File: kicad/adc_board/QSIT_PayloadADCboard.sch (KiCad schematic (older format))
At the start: 34 parts, among them J1 Conn_02x05_Odd_Even, J2 Conn_02x05_Odd_Even, J3 Conn_02x05_Odd_Even, U1 MCP3561_4CH, U2 NCP1117-3.3_SOT223

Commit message: changed to single 9pin connector
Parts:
- removed J1, J2, J3: Conn_02x05_Odd_Even, Connector_PinSocket_1.27mm:PinSocket_2x05_P1.27mm_Vertical_SMD, symbol Connector_Generic:Conn_02x05_Odd_Even
- removed JP1, JP2, JP3: bridge, Jumper:SolderJumper-3_P1.3mm_Open_RoundedPad1.0x1.5mm, symbol Jumper:Jumper_3_Bridged12
- removed U1: MCP3561_4CH, Package_SO:TSSOP-20_4.4x6.5mm_P0.65mm, symbol A_Tale_Of_A_Library:MCP3561_4CH
- removed U2: NCP1117-3.3_SOT223, Package_TO_SOT_SMD:SOT-223-3_TabPin2, symbol Regulator_Linear:NCP1117-3.3_SOT223
- removed VR1: LM4040D25FTA, digikey-footprints:SOT-23-3, symbol dk_PMIC-Voltage-Reference:LM4040D25FTA
- added C10, C11, C12, C13, C14, C15, C9: 100nF, Capacitor_SMD:C_0603_1608Metric_Pad1.05x0.95mm_HandSolder, symbol Device:C
- added C16, C18: 4u7, Capacitor_THT:CP_Radial_D4.0mm_P2.00mm, symbol Device:CP
- added C17: 2u2, Capacitor_THT:CP_Radial_D4.0mm_P2.00mm, symbol Device:CP
- added C? (x2): 12p, Capacitor_SMD:C_0603_1608Metric_Pad1.05x0.95mm_HandSolder, symbol Device:C
- added D1, D2: LED, LED_SMD:LED_0805_2012Metric_Pad1.15x1.40mm_HandSolder, symbol Device:LED
- added J1: Conn_01x09, Connector_PinHeader_2.54mm:PinHeader_1x09_P2.54mm_Vertical, symbol Connector_Generic:Conn_01x09
- added J2: Power_Conn, TerminalBlock_4Ucon:TerminalBlock_4Ucon_1x02_P3.50mm_Horizontal, symbol Connector:Screw_Terminal_01x02
- added J4: Conn_ARM_JTAG_SWD_10, Connector_PinHeader_1.27mm:PinHeader_2x05_P1.27mm_Vertical_SMD, symbol Connector:Conn_ARM_JTAG_SWD_10
- added J5: Conn_01x03, Connector_PinHeader_2.54mm:PinHeader_1x03_P2.54mm_Vertical, symbol Connector_Generic:Conn_01x03
- added J6: Conn_02x05_Odd_Even, Connector_PinSocket_1.27mm:PinSocket_2x05_P1.27mm_Vertical_SMD, symbol Connector_Generic:Conn_02x05_Odd_Even
- added R12, R13, R16, R19, R? (x2): 10k, Resistor_SMD:R_0603_1608Metric_Pad1.05x0.95mm_HandSolder, symbol Device:R
- added R14, R15: 10R, Resistor_SMD:R_0603_1608Metric_Pad1.05x0.95mm_HandSolder, symbol Device:R
- added R17, R18: 330R, Resistor_SMD:R_0603_1608Metric_Pad1.05x0.95mm_HandSolder, symbol Device:R
- added SW1: SW_Push, Button_Switch_SMD:SW_Push_1P1T_NO_CK_KMR2, symbol Switch:SW_Push
- added U1: MCP3564, Package_SO:TSSOP-20_4.4x6.5mm_P0.65mm, symbol A_Tale_Of_A_Library:MCP3564
- added U2: MAX6070, Package_TO_SOT_SMD:SOT-23-6_Handsoldering, symbol A_Tale_Of_A_Library:MAX6070
- added U3: STM32F373CCT6, Package_QFP:LQFP-48_7x7mm_P0.5mm, symbol MCU_ST_STM32F3:STM32F373CCTx
- added U4: TC1108-3.3VDBTR, Package_TO_SOT_SMD:SOT-223-3_TabPin2, symbol Regulator_Linear:LT1129-3.3_SOT223
- added U5: MPE1205S-1W, A_Tale_Of_A_Library:Converter_DCDC_multicorp_THT, symbol A_Tale_Of_A_Library:MPE1205S-1W
- added X?: ECS-2520MVLC-049-BN, Oscillator:Oscillator_SMD_ECS_2520MV-xxx-xx-4Pin_2.5x2.0mm, symbol Oscillator:ECS-2520MV-xxx-xx
- added Y?: 8MHz, symbol Device:Crystal
- C1, C2, C3, C4, C5, C6, C7, C8: Type (none) -> X7R; Voltage (none) -> 16V
- R1: value R -> 10R
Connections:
- net labels added: +12V, ADC_CH1, ADC_CH2, ADC_CH3, ADC_CH4, BOOT0, BOOT1, FCLK_X, FCLK_Y, LED1, LED2, MEMS_OUT_EN, SPI1_CS, SPI1_MISO, SPI1_MOSI, SPI1_SCK, SPI1_~IRQ~, SPI2_CS, SPI2_MOSI, SPI2_SCK, SWCLK, SWDIO, TIM14_CH1, TIM16_CH1, TIM17_CH1, USART2_RX, USART2_TX, VAA, ~RST
- net labels removed: MISO, MOSI, SCK, U_signal, X1a, X2a, X_signal, Y1a, Y2a, Y_signal, ~CS, ~IRQ
- wire segments 95 -> 187
- no-connect marks 2 -> 5
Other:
- note added: "2.5V Reference"
- note added: "2.5V ±2ppm/°C"
- note added: "240 Hz x 60 = 14.4 kHz"
- note added: "300mA out"
- note added: "9P flat cable"
- note added: "ARM SWD Connector"
- note added: "Analog"
- note added: "Debug"
- note added: "Input Voltage\n10.8 ... 13.2"
- note added: "MCLK 4.9152 MHz generator"
- note added: "MCU"
- note added: "MEMS Driver"
- note added: "MPE1205S-1W\nIsol. DC/DC, THT, 1 W, +/-5 V, 100mA\n"
- note added: "Mechanical"
- note added: "Power"
- note added: "UART (Debug)"
- note added: "add power switch for MEMS driver?"
- note added: "pinout see:\nMirrorcle BDQ PicoAmp 4.6 User Guide.pdf"
- note removed: "- check ISE for 2.5 reference\n- check ISE for +/- 5V DC source\n- check ISE for 3.3V regulator\n- find out, if more stuff fits on a larger PCB\n- research Pinout of Mirrorcle Board"
- note removed: "60uA ... 15mA bias current"
- note removed: "The LM4040 does not require an external stabilizing \ncapacitor while ensuring stability with any capacitive load."
- note removed: "do not use STM32 (not in stock)\ndo not use internal ADCs because min. 14 Bit resolution is required\nuse flat cable to connect to a Teensy breakout board"
- moved on the sheet: C1, C2, C3, C4, C5, C6, C7, C8, FB1, H1, H2, H3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

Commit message: STM32 board ready for review
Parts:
- removed R3: 10R, Resistor_SMD:R_0603_1608Metric_Pad1.05x0.95mm_HandSolder, symbol Device:R
- removed R?: 10k, Resistor_SMD:R_0603_1608Metric_Pad1.05x0.95mm_HandSolder, symbol Device:R
- removed Y?: 8MHz, symbol Device:Crystal
- added TP1: TestPoint, TestPoint:TestPoint_Keystone_5000-5004_Miniature, symbol Connector:TestPoint
- added Y1: Crystal_GND24, Crystal:Crystal_SMD_TXC_7M-4Pin_3.2x2.5mm, symbol Device:Crystal_GND24
- gave numbers to parts that had none: 4
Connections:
- net BOOT0: now also TP1.1
- net GND: now also Y1.2, Y1.4
- net MCLK: now also U1.18 (MCLKIN)
- net MEMS_OUT_EN: now also U3.29 (PA8)
- net at C19.1, U3.5 (PF0): now also Y1.1
- net at C20.1, U3.6 (PF1): now also Y1.3
- net BOOT1: no longer names the net of U3.20 (PB2)
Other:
- note added: "BOOT1 BOOT0 \n x 0 flash memory\n 0 1 system memory\n 1 1 embedded SRAM"
- note added: "double check pinout"
- note added: "https://www.digikey.ch/de/products/detail/olimex-ltd/ARM-JTAG-20-10/3471401"
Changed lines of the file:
@@
 	0    -1   -1   0
 $EndComp
-$Comp
-L Device:R R3
-U 1 1 61A6A943
-P 7700 1150
-F 0 "R3" V 7750 1350 50  0000 C CNN
-F 1 "10R" V 7700 1150 50  0000 C CNN
-F 2 "Resistor_SMD:R_0603_1608Metric_Pad1.05x0.95mm_HandSolder" V 7630 1150 50  0001 C CNN
-F 3 "~" H 7700 1150 50  0001 C CNN
-	1    7700 1150
-	0    -1   -1   0
-$EndComp
 Wire Wire Line
 	1100 6250 1100 6200
@@
 Wire Wire Line
 	5050 5500 4850 5500
-Text GLabel 7150 5000 2    50   Input ~ 0
-BOOT1
 Wire Wire Line
 	6450 4900 6650 4900
@@
 9P flat cable
 $Comp
-L Device:R R?
+L Device:R R20
 U 1 1 623954BA
 P 4750 3550
-F 0 "R?" H 4900 3600 50  0000 L CNN
+F 0 "R20" H 4900 3600 50  0000 L CNN
 F 1 "10k" H 4820 3505 50  0000 L CNN
 F 2 "Resistor_SMD:R_0603_1608Metric_Pad1.05x0.95mm_HandSolder" V 4680 3550 50  0001 C CNN
@@
 Wire Wire Line
 	5050 3400 4750 3400
-Wire Wire Line
-	4750 3400 4550 3400
 Connection ~ 4750 3400
 $Comp
-L power:GND #PWR?
+L power:GND #PWR041
 U 1 1 623ABA27
 P 4750 3700
-F 0 "#PWR?" H 4750 3450 50  0001 C CNN
+F 0 "#PWR041" H 4750 3450 50  0001 C CNN
 F 1 "GND" H 4850 3550 50  0000 R CNN
 F 2 "" H 4750 3700 50  0001 C CNN
@@
 	1    0    0    -1
 $EndComp
-Text GLabel 4550 3400 0    50   Input ~ 0
+Text GLabel 4300 3400 0    50   Input ~ 0
 BOOT0
-$Comp
-L Device:R R?
-U 1 1 623C7134
-P 6900 5100
-F 0 "R?" V 6850 5250 50  0000 L CNN
-F 1 "10k" V 6900 5050 50  0000 L CNN
-F 2 "Resistor_SMD:R_0603_1608Metric_Pad1.05x0.95mm_HandSolder" V 6830 5100 50  0001 C CNN
-F 3 "~" H 6900 5100 50  0001 C CNN
-	1    6900 5100
-	0    1    -1   0
-$EndComp
-Wire Wire Line
-	6750 5100 6700 5100
-Wire Wire Line
-	6700 5100 6650 5050
-Wire Wire Line
-	7050 5100 7250 5100
-$Comp
-L power:GND #PWR?
-U 1 1 623E97D1
-P 7250 5100
-F 0 "#PWR?" H 7250 4850 50  0001 C CNN
-F 1 "GND" V 7250 4950 50  0000 R CNN
-F 2 "" H 7250 5100 50  0001 C CNN
-F 3 "" H 7250 5100 50  0001 C CNN
-	1    7250 5100
-	0    -1   -1   0
-$EndComp
 Text Notes 1250 3500 0    50   ~ 0
 MCLK 4.9152 MHz generator
 $Comp
-L Oscillator:ECS-2520MV-xxx-xx X?
+L Oscillator:ECS-2520MV-xxx-xx X1
 U 1 1 61AAE6AA
 P 1150 3750
-F 0 "X?" H 1550 3600 50  0000 L CNN
+F 0 "X1" H 1550 3600 50  0000 L CNN
 F 1 "ECS-2520MVLC-049-BN" H 1300 3450 50  0000 L CNN
 F 2 "Oscillator:Oscillator_SMD_ECS_2520MV-xxx-xx-4Pin_2.5x2.0mm" H 1600 3400 50  0001 C CNN
@@
 $EndComp
 $Comp
-L power:+3V3 #PWR?
+L power:+3V3 #PWR040
 U 1 1 61AB5159
 P 1150 3450
-F 0 "#PWR?" H 1150 3300 50  0001 C CNN
+F 0 "#PWR040" H 1150 3300 50  0001 C CNN
 F 1 "+3V3" H 1150 3600 50  0000 C CNN
 F 2 "" H 1150 3450 50  0001 C CNN
@@
 $EndComp
 $Comp
-L power:GND #PWR?
+L power:GND #PWR042
 U 1 1 61AB6346
 P 1150 4050
-F 0 "#PWR?" H 1150 3800 50  0001 C CNN
+F 0 "#PWR042" H 1150 3800 50  0001 C CNN
 F 1 "GND" H 1250 3900 50  0000 R CNN
 F 2 "" H 1150 4050 50  0001 C CNN
@@
 NoConn ~ 750  3750
 Wire Wire Line
-	7450 1150 7550 1150
-Wire Wire Line
 	7450 1250 7950 1250
 Wire Wire Line
@@
 	7950 1450 7450 1450
 Wire Wire Line
-	7850 1150 8250 1150
-Wire Wire Line
 	8250 1350 7850 1350
 Wire Wire Line
@@
 	2950 5200 2700 5200
 $Comp
-L Device:Crystal Y?
-U 1 1 61DA8492
-P 4400 4450
-F 0 "Y?" V 4354 4581 50  0000 L CNN
-F 1 "8MHz" V 4445 4581 50  0000 L CNN
-F 2 "" H 4400 4450 50  0001 C CNN
-F 3 "~" H 4400 4450 50  0001 C CNN
-	1    4400 4450
-	0    1    1    0
-$EndComp
-$Comp
-L Device:C C?
+L Device:C C19
 U 1 1 61DC61B7
 P 4200 4300
-F 0 "C?" V 4000 4450 50  0000 C CNN
+F 0 "C19" V 4000 4450 50  0000 C CNN
 F 1 "12p" V 4100 4450 50  0000 C CNN
 F 2 "Capacitor_SMD:C_0603_1608Metric_Pad1.05x0.95mm_HandSolder" H 4238 4150 50  0001 C CNN
@@
 $EndComp
 $Comp
-L Device:C C?
+L Device:C C20
 U 1 1 61DC7D49
 P 4200 4600
-F 0 "C?" V 4000 4750 50  0000 C CNN
+F 0 "C20" V 4000 4750 50  0000 C CNN
 F 1 "12p" V 4100 4750 50  0000 C CNN
 F 2 "Capacitor_SMD:C_0603_1608Metric_Pad1.05x0.95mm_HandSolder" H 4238 4450 50  0001 C CNN
@@
 $EndComp
 Wire Wire Line
-	4400 4600 4350 4600
-Wire Wire Line
-	4400 4300 4350 4300
-Wire Wire Line
 	4050 4300 4050 4450
 $Comp
-L power:GND #PWR?
+L power:GND #PWR043
 U 1 1 61DE5BC5
 P 4050 4450
-F 0 "#PWR?" H 4050 4200 50  0001 C CNN
+F 0 "#PWR043" H 4050 4200 50  0001 C CNN
 F 1 "GND" V 4050 4300 50  0000 R CNN
 F 2 "" H 4050 4450 50  0001 C CNN
@@
 Wire Wire Line
 	4050 4450 4050 4600
-Connection ~ 4400 4600
 $Comp
 L MCU_ST_STM32F3:STM32F373CCTx U3
@@
 $EndComp
 Wire Wire Line
-	5050 4700 4900 4700
-Wire Wire Line
-	4900 4700 4850 4650
-Wire Wire Line
-	4850 4650 4850 4350
-Wire Wire Line
-	4850 4350 4800 4300
-Wire Wire Line
-	4800 4300 4400 4300
-Connection ~ 4400 4300
-Wire Wire Line
 	4700 4600 4750 4650
 Wire Wire Line
@@
 Wire Wire Line
 	4800 4800 5050 4800
-Wire Wire Line
-	4400 4600 4700 4600
 NoConn ~ 1600 1450
 NoConn ~ 1600 1550
@@
 Wire Notes Line
 	600  7700 3300 7700
-Wire Wire Line
-	6450 5000 6650 5000
-Wire Wire Line
-	6650 5050 6650 5000
-Connection ~ 6650 5000
-Wire Wire Line
-	6650 5000 7150 5000
 Wire Notes Line
 	11100 6450 11100 4900
@@
 Mechanical
 $Comp
-L Graphic:SYM_Flash_Small #SYM?
+L Graphic:SYM_Flash_Small #SYM1
 U 1 1 62104C7E
 P 8150 5350
-F 0 "#SYM?" V 8060 5350 50  0001 C CNN
+F 0 "#SYM1" V 8060 5350 50  0001 C CNN
 F 1 "SYM_Flash_Small" V 8240 5350 50  0001 C CNN
 F 2 "" H 8150 5325 50  0001 C CNN
@@
 	1    0    0    -1
 $EndComp
+Wire Notes Line style solid
+	3700 3000 3700 3300
+Text Notes 3450 3300 0    50   ~ 0
+BOOT1 BOOT0 \n   x     0     flash memory\n   0     1     system memory\n   1     1     embedded SRAM
+Wire Notes Line style solid
+	4000 3000 4000 3300
+Wire Notes Line style solid
+	3450 3050 4650 3050
+$Comp
+L Connector:TestPoint TP1
+U 1 1 61B364E0
+P 4300 3500
+F 0 "TP1" V 4200 3600 50  0000 C CNN
+F 1 "TestPoint" V 4404 3572 50  0001 C CNN
+F 2 "TestPoint:TestPoint_Keystone_5000-5004_Miniature" H 4500 3500 50  0001 C CNN
+F 3 "~" H 4500 3500 50  0001 C CNN
+	1    4300 3500
+	0    -1   -1   0
+$EndComp
+Wire Wire Line
+	4300 3400 4450 3400
+Wire Wire Line
+	4300 3500 4350 3500
+Wire Wire Line
+	4350 3500 4450 3400
+Connection ~ 4450 3400
+Wire Wire Line
+	4450 3400 4750 3400
+Text Notes 1300 2300 0    39   ~ 0
+https://www.digikey.ch/de/products/detail/olimex-ltd/ARM-JTAG-20-10/3471401
+Text Notes 1650 1800 0    50   ~ 0
+double check pinout
+$Comp
+L Device:Crystal_GND24 Y1
+U 1 1 61C03ABE
+P 4450 4450
+F 0 "Y1" V 4650 4550 50  0000 L CNN
+F 1 "Crystal_GND24" V 4200 4500 50  0000 L CNN
+F 2 "Crystal:Crystal_SMD_TXC_7M-4Pin_3.2x2.5mm" H 4450 4450 50  0001 C CNN
+F 3 "~" H 4450 4450 50  0001 C CNN
+	1    4450 4450
+	0    1    1    0
+$EndComp
+Wire Wire Line
+	4350 4300 4450 4300
+Wire Wire Line
+	4350 4600 4450 4600
+Connection ~ 4450 4300
+Connection ~ 4450 4600
+Wire Wire Line
+	4250 4450 4050 4450
+Wire Wire Line
+	4450 4600 4700 4600
+$Comp
+L power:GND #PWR044
+U 1 1 61C17303
+P 4650 4450
+F 0 "#PWR044" H 4650 4200 50  0001 C CNN
+F 1 "GND" V 4650 4350 50  0000 R CNN
+F 2 "" H 4650 4450 50  0001 C CNN
+F 3 "" H 4650 4450 50  0001 C CNN
+	1    4650 4450
+	0    -1   -1   0
+$EndComp
+Wire Wire Line
+	5050 4700 5000 4700
+Wire Wire Line
+	5000 4700 4950 4650
+Wire Wire Line
+	4950 4650 4950 4350
+Wire Wire Line
+	4950 4350 4900 4300
+Wire Wire Line
+	4450 4300 4900 4300
+Wire Wire Line
+	7450 1150 8250 1150
+Text GLabel 6650 3900 2    50   Input ~ 0
+MEMS_OUT_EN
+Wire Wire Line
+	6650 3900 6450 3900
 $EndSCHEMATC

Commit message: further pcb improvements
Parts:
- removed C16, C18: 4u7, Capacitor_THT:CP_Radial_D4.0mm_P2.00mm, symbol Device:CP
- removed U1: MCP3564, Package_SO:TSSOP-20_4.4x6.5mm_P0.65mm, symbol A_Tale_Of_A_Library:MCP3564
- removed U2: MAX6070, Package_TO_SOT_SMD:SOT-23-6_Handsoldering, symbol A_Tale_Of_A_Library:MAX6070
- removed U5: MPE1205S-1W, A_Tale_Of_A_Library:Converter_DCDC_multicorp_THT, symbol A_Tale_Of_A_Library:MPE1205S-1W
- added C16, C18, C21: 4u7, Capacitor_SMD:C_1206_3216Metric, symbol Device:C
- added C22: 100nF, Capacitor_SMD:C_0603_1608Metric, symbol Device:C
- added U1: MCP3564, Package_SO:TSSOP-20_4.4x6.5mm_P0.65mm, symbol simonmartin_kicad_lib:MCP3564
- added U2: MAX6070, Package_TO_SOT_SMD:SOT-23-6_Handsoldering, symbol simonmartin_kicad_lib:MAX6070
- added U5: MPE1205S-1W, simonmartin_kicad_lib:Converter_DCDC_multicorp_THT, symbol simonmartin_kicad_lib:MPE1205S-1W
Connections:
- net +12V: now also U5.1 (Vin)
- net +2V5: now also U1.4 (REF+), U2.5 (OUTS), U2.6 (OUTF)
- net +3V3: now also C21.2, U1.20 (DVDD)
- net +5V: now also C16.2, U5.7 (+Vo)
- net -5V: now also C18.1, U5.5 (-Vo)
- net GND: now also J5.1 (Pin_1), C16.1, C18.2, C21.1, C22.1, U1.10 (CH5), U1.12 (CH7), U1.19 (DGND), U1.2 (AGND), U1.3 (REF-), U1.6 (CH1), U1.8 (CH3), U2.2 (GND), U5.2 (GND), U5.6 (0V); no longer J5.3 (Pin_3)
- net LED1: now also U3.43 (PB7)
- net LED2: now also U3.42 (PB6)
- net MCLK: now also U1.18 (MCLKIN)
- net USART2_TX: now also J5.3 (Pin_3); no longer J5.1 (Pin_1)
- net VAA: now also C22.2, U1.1 (AVDD), U2.3 (EN), U2.4 (IN)
- net at C3.2, R2.1: now also U1.5 (CH0)
- net at C4.2, R7.1: now also U1.7 (CH2)
- net at C5.2, R10.1: now also U1.9 (CH4)
- net at C6.2, R11.1: now also U1.11 (CH6)
- net at R9.2: now also U1.13 (~CS~)
- net at R8.2: now also U1.14 (SCK)
- net at R6.2: now also U1.15 (SDI)
- net at R5.2: now also U1.16 (SDO)
- net at R4.2: now also U1.17 (~IRQ~/MDAT)
- net at C11.2: now also U2.1 (FILT)
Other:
- note added: "MAX6070\n- FP: ok\n- Sch: ok"
- note added: "MCP3564\n- FP: ok\n- Sch:"
- note added: "TIM14_CH1"
- note added: "TIM16_CH1"
- note removed: "240 Hz x 60 = 14.4 kHz"
- note removed: "double check pinout"
- note removed: "https://www.digikey.ch/de/products/detail/olimex-ltd/ARM-JTAG-20-10/3471401"
- moved on the sheet: C1, C10, C11, C19, C2, C20, C3, C4, C5, C6, FB1, J1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

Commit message: rev.1 of ADC board
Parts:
- J6: footprint Connector_PinSocket_1.27mm:PinSocket_2x05_P1.27mm_Vertical_SMD -> Connector_PinHeader_1.27mm:PinHeader_2x05_P1.27mm_Vertical_SMD

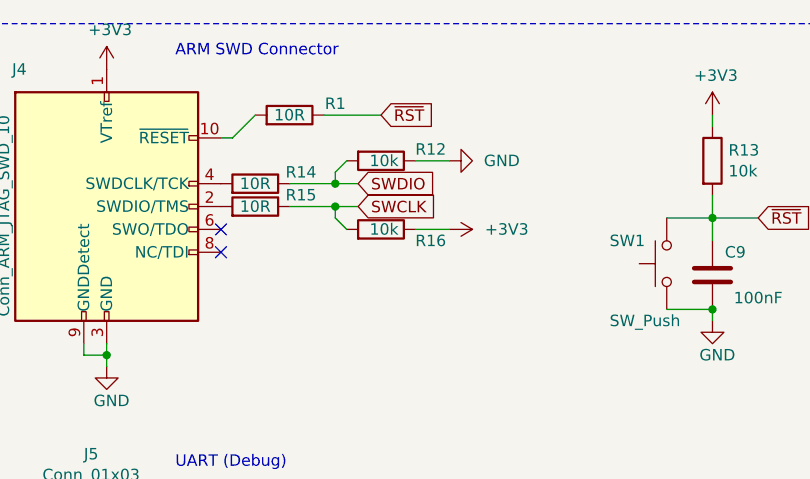
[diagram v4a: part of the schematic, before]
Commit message: SWDIO/SWCLK swapped
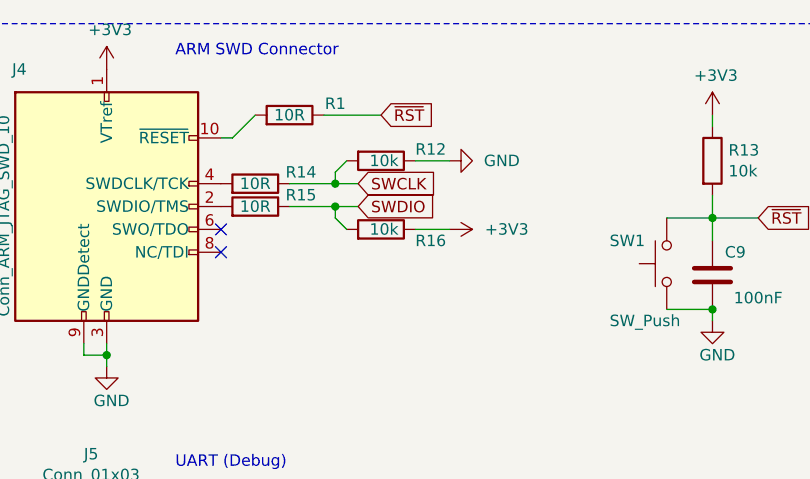
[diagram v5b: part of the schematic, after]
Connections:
- net SWCLK: now also R12.2, R14.1; no longer R15.1, R16.2
- net SWDIO: now also R15.1, R16.2; no longer R12.2, R14.1
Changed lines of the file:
@@
 Wire Wire Line
 	2300 950  2050 950
+Text GLabel 2200 1350 2    50   Input ~ 0
+SWDIO
 Text GLabel 2200 1250 2    50   Input ~ 0
-SWDIO
-Text GLabel 2200 1350 2    50   Input ~ 0
 SWCLK
 $Comp

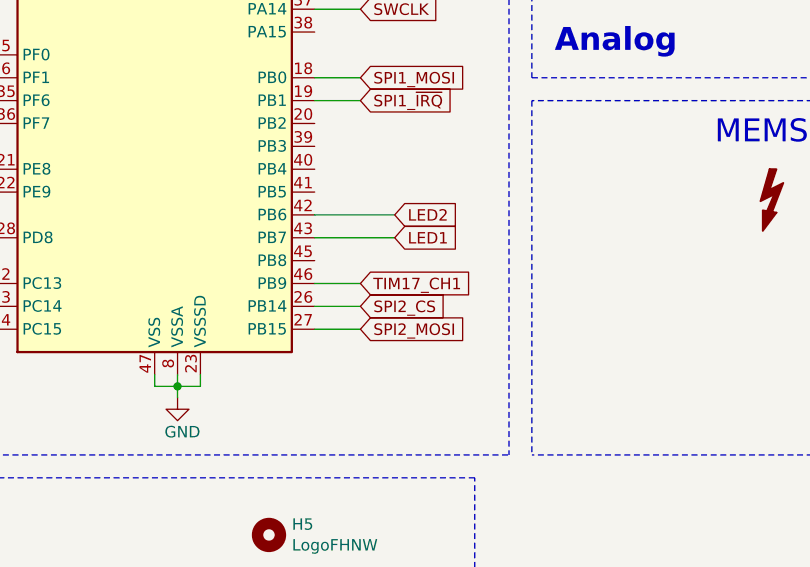
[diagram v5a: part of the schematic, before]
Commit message: fixed wrong connection to PSD X/Y axis
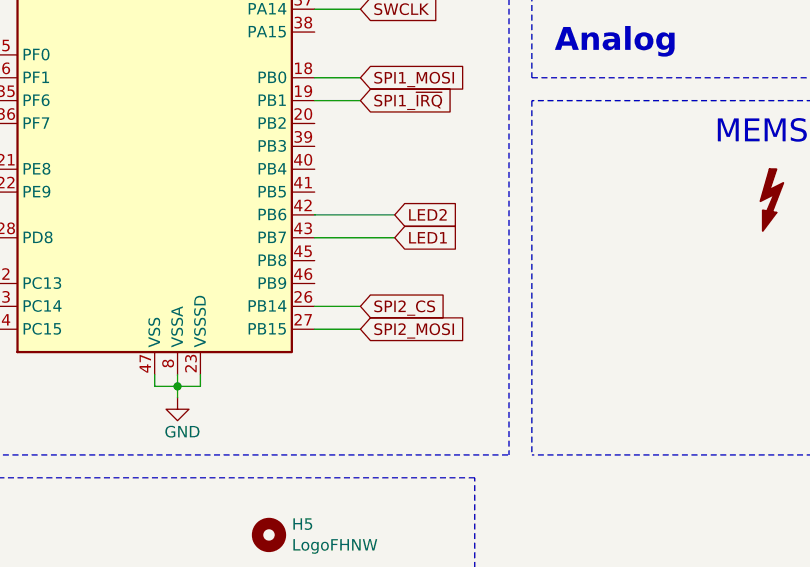
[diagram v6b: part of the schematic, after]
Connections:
- net TIM17_CH1: no longer names the net of U3.46 (PB9)
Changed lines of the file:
@@
 LED1
-Wire Wire Line
-	6350 5700 6150 5700
-Text GLabel 6350 5700 2    50   Input ~ 0
-TIM17_CH1
 Wire Wire Line
 	6150 4500 6350 4500
